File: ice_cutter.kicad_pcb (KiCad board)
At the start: 4 copper layers, 90 x 100 mm, 184 parts, among them J1 Conn_01x01_Male, J2 Barrel_Jack, J3 pot, J4 Conn_01x01_Male, J5 program, J6 program2, J7 hands, J8 UART, J9 xt60, M1 Motor_Servo, M2 Motor_Servo, Q1 Q_PMOS_GSD, Q10 S8050_SMD, Q11 Q_NMOS_GSD, Q12 Q_NMOS_GSD, Q13 Q_NMOS_GSD, Q14 Q_NMOS_GSD, Q15 S8550, Q16 S8050_SMD, Q17 S8050_SMD, Q18 S8050_SMD, Q2 Q_PMOS_GSD, Q3 Q_PMOS_GSD, Q4 S8550, Q5 Q_NMOS_GSD, Q6 S8550, Q7 Q_NMOS_GSD, Q8 S8050_SMD, Q9 S8050_SMD, SW1 SW_Push, SW2 SW_Push, SW3 SW_Push, U1 LM317_TO-252, U10 TMP117, U11 TM1620, U12 INA219AxD, U2 LM317_TO-252, U3 INA219AxD, U4 LM317_TO-252, U5 INA219AxD, U6 FJ4301AH, U7 FJ4301AH, U8 STM32G030XX, U9 SHT30-DIS

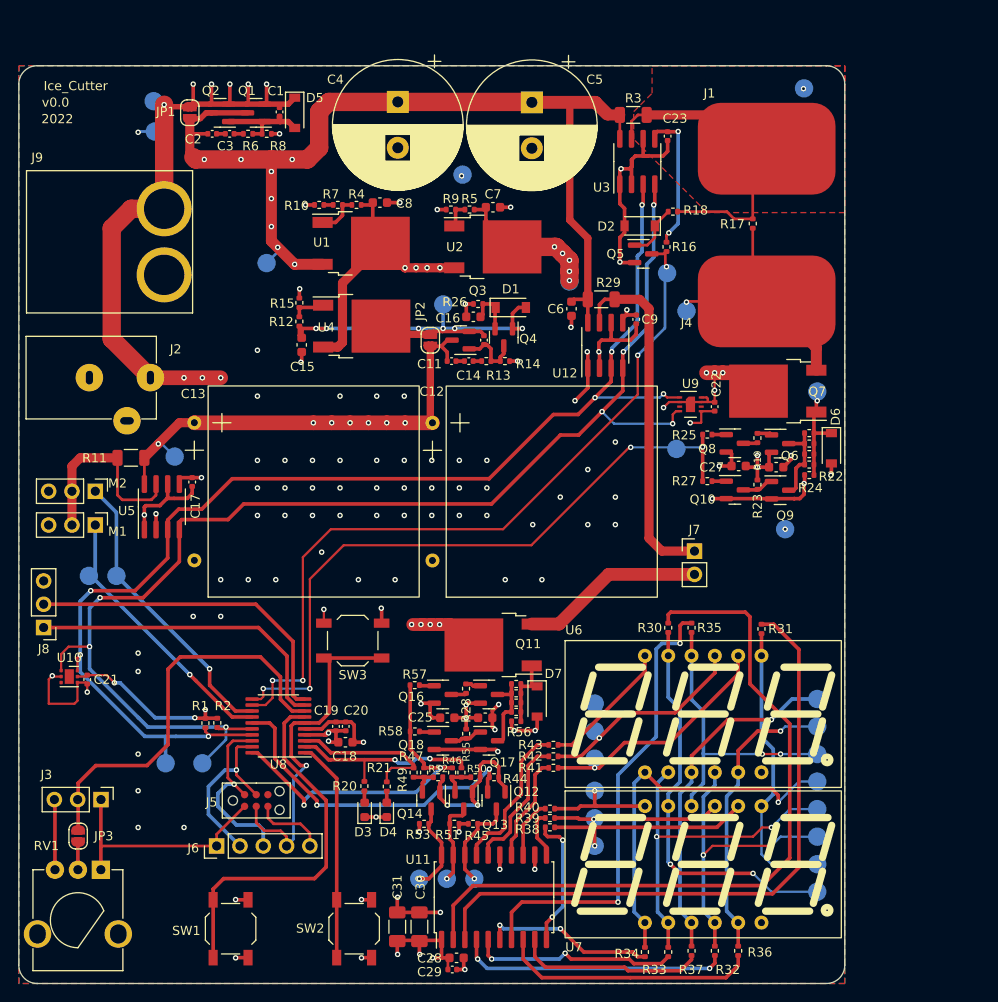
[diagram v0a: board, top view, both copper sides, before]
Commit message: improved schematic and changed the shunt resistors
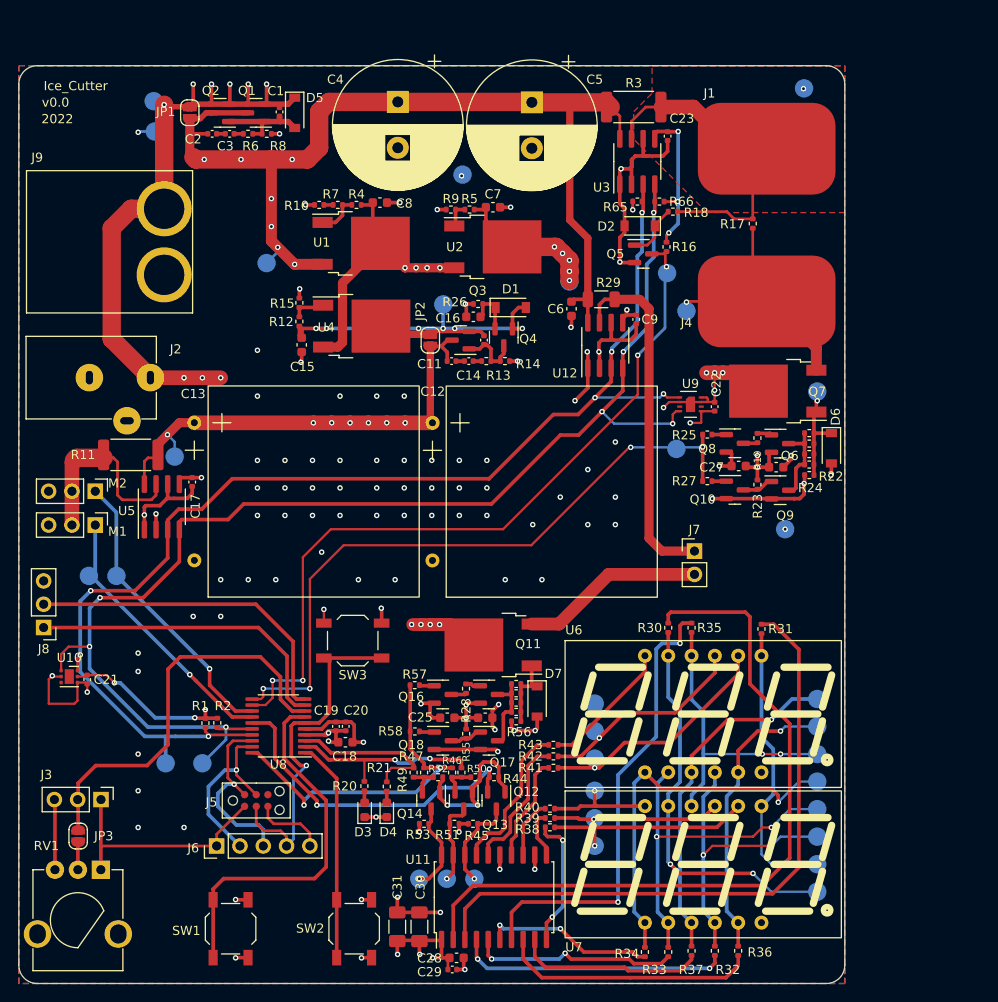
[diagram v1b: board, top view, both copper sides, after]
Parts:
- added R65: 4k7, Resistor_SMD:R_0402_1005Metric, F.Cu at (135.8, 44.2)
- added R66: 4k7, Resistor_SMD:R_0402_1005Metric, F.Cu at (138.2, 44.2)
- C4, C5: value 1m -> 4.7m
- R11, R3: value 0R1 -> 15mR; footprint Resistor_SMD:R_1206_3216Metric -> Resistor_SMD:R_2512_6332Metric
- R18: value 100R -> 330R
- moved R3 0.86 mm to (135.4, 33.9)
- moved R11 0.32 mm to (80.6, 71.8)
- turned R18 to 180 degrees
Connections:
- R18 pad 1: Net-(D2-Pad1) -> /Wire_H
- R18 pad 2: /Wire_H -> Net-(D2-Pad1)
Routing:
- net +3V3: track 155.8 -> 158.4 mm, vias 20 -> 22
- net /5V_SS: track 67.0 -> 68.0 mm
- net /Wire_H: track 35.3 -> 36.0 mm
- net /V_SS: track 111.8 -> 111.9 mm, vias 8 -> 7

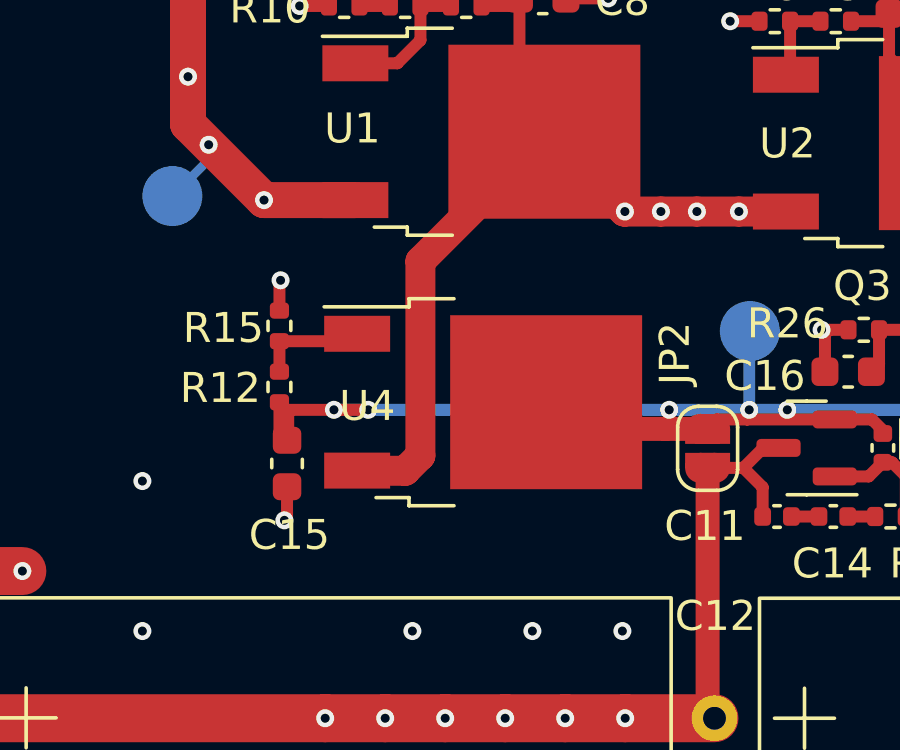
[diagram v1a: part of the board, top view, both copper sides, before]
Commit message: modified the system to operate on 5V - bypassed all regs and changed the BIG FET to a lower threshold V
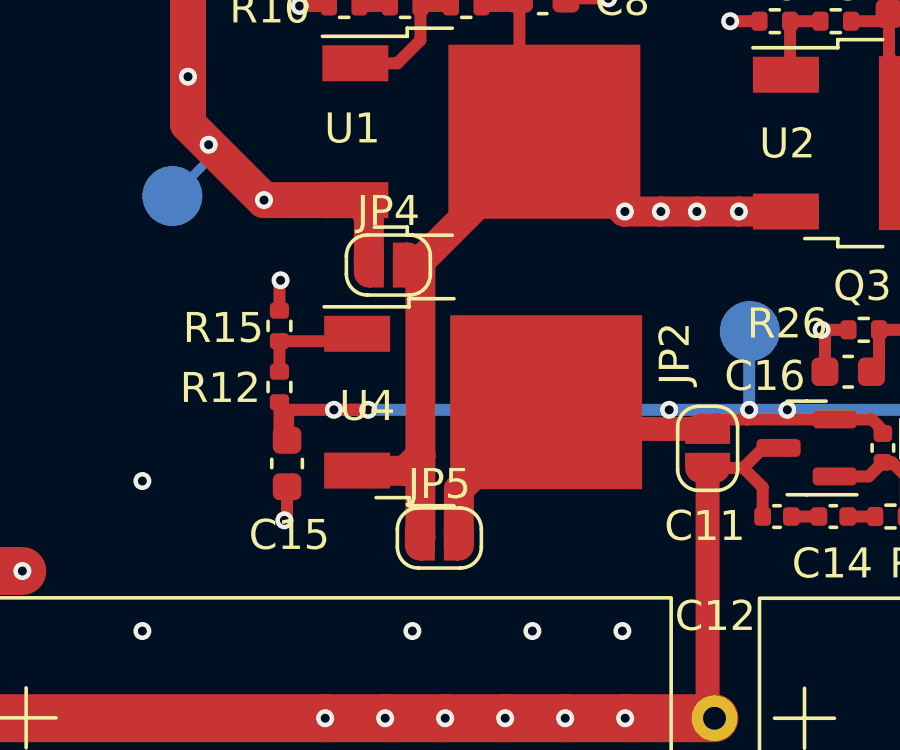
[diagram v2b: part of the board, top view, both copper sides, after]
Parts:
- added JP4: Jumper_2_Open, Jumper:SolderJumper-2_P1.3mm_Open_RoundedPad1.0x1.5mm, F.Cu at (102.6, 53.2)
- added JP5: Jumper_2_Open, Jumper:SolderJumper-2_P1.3mm_Open_RoundedPad1.0x1.5mm, F.Cu at (104.3, 62.3)
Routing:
- net +5V: track 47.7 -> 53.4 mm
- net +12V: track 149.2 -> 151.9 mm
- net /V_SS: track 111.9 -> 114.2 mm
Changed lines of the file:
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@@
     )
   )
+  (footprint "Jumper:SolderJumper-2_P1.3mm_Open_RoundedPad1.0x1.5mm" (layer "F.Cu")
+    (at 102.564 53.213)
+    (descr "SMD Solder Jumper, 1x1.5mm, rounded Pads, 0.3mm gap, open")
+    (tags "solder jumper open")
+    (property "Extended" "0")
+    (property "Populate" "No")
+    (property "Sheetfile" "ice_cutter.kicad_sch")
+    (property "Sheetname" "")
+    (attr exclude_from_pos_files)
+    (fp_text reference "JP4" (at 0 -1.8) (layer "F.SilkS")
+      (effects (font (size 1 1) (thickness 0.15)))
+    )
+    (fp_text value "Jumper_2_Open" (at 0 1.9) (layer "F.Fab")
+      (effects (font (size 1 1) (thickness 0.15)))
+    )
+    (fp_line (start -1.4 0.3) (end -1.4 -0.3) (layer "F.SilkS") (width 0.12))
+    (fp_line (start 1.4 -0.3) (end 1.4 0.3) (layer "F.SilkS") (width 0.12))
+    (fp_line (start -0.7 -1) (end 0.7 -1) (layer "F.SilkS") (width 0.12))
+    (fp_line (start 0.7 1) (end -0.7 1) (layer "F.SilkS") (width 0.12))
+    (fp_arc (start -1.4 -0.3) (mid -1.194975 -0.794975) (end -0.7 -1) (layer "F.SilkS") (width 0.12))
+    (fp_arc (start -0.7 1) (mid -1.194975 0.794975) (end -1.4 0.3) (layer "F.SilkS") (width 0.12))
+    (fp_arc (start 1.4 0.3) (mid 1.194975 0.794975) (end 0.7 1) (layer "F.SilkS") (width 0.12))
+    (fp_arc (start 0.7 -1) (mid 1.194975 -0.794975) (end 1.4 -0.3) (layer "F.SilkS") (width 0.12))
+    (fp_line (start -1.65 -1.25) (end 1.65 -1.25) (layer "F.CrtYd") (width 0.05))
+    (fp_line (start 1.65 1.25) (end -1.65 1.25) (layer "F.CrtYd") (width 0.05))
+    (fp_line (start -1.65 -1.25) (end -1.65 1.25) (layer "F.CrtYd") (width 0.05))
+    (fp_line (start 1.65 1.25) (end 1.65 -1.25) (layer "F.CrtYd") (width 0.05))
+    (pad "1" smd custom locked (at -0.65 0) (size 1 0.5) (layers "F.Cu" "F.Mask")
+      (net 3 "/V_SS") (pinfunction "A") (pintype "passive") (zone_connect 2)
+      (options (clearance outline) (anchor rect))
+      (primitives
+        (gr_circle (center 0 0.25) (end 0.5 0.25) (width 0) (fill yes))
+        (gr_circle (center 0 -0.25) (end 0.5 -0.25) (width 0) (fill yes))
+        (gr_poly (pts
+            (xy 0.5 0.75)
+            (xy 0 0.75)
+            (xy 0 -0.75)
+            (xy 0.5 -0.75)
+          ) (width 0) (fill yes))
+      ))
+    (pad "2" smd custom locked (at 0.65 0) (size 1 0.5) (layers "F.Cu" "F.Mask")
+      (net 8 "+12V") (pinfunction "B") (pintype "passive") (zone_connect 2)
+      (options (clearance outline) (anchor rect))
+      (primitives
+        (gr_circle (center 0 0.25) (end 0.5 0.25) (width 0) (fill yes))
+        (gr_circle (center 0 -0.25) (end 0.5 -0.25) (width 0) (fill yes))
+        (gr_poly (pts
+            (xy 0 0.75)
+            (xy -0.5 0.75)
+            (xy -0.5 -0.75)
+            (xy 0 -0.75)
+          ) (width 0) (fill yes))
+      ))
+  )
   (footprint "Capacitor_THT:CP_Radial_D14.0mm_P5.00mm" (layer "F.Cu")
     (at 124.265 33.401 -90)
@@
     )
   )
+  (footprint "Jumper:SolderJumper-2_P1.3mm_Open_RoundedPad1.0x1.5mm" (layer "F.Cu")
+    (at 104.264 62.313)
+    (descr "SMD Solder Jumper, 1x1.5mm, rounded Pads, 0.3mm gap, open")
+    (tags "solder jumper open")
+    (property "Extended" "0")
+    (property "Populate" "No")
+    (property "Sheetfile" "ice_cutter.kicad_sch")
+    (property "Sheetname" "")
+    (attr exclude_from_pos_files)
+    (fp_text reference "JP5" (at 0 -1.8) (layer "F.SilkS")
+      (effects (font (size 1 1) (thickness 0.15)))
+    )
+    (fp_text value "Jumper_2_Open" (at 0 1.9) (layer "F.Fab")
+      (effects (font (size 1 1) (thickness 0.15)))
+    )
+    (fp_line (start -1.4 0.3) (end -1.4 -0.3) (layer "F.SilkS") (width 0.12))
+    (fp_line (start 0.7 1) (end -0.7 1) (layer "F.SilkS") (width 0.12))
+    (fp_line (start 1.4 -0.3) (end 1.4 0.3) (layer "F.SilkS") (width 0.12))
+    (fp_line (start -0.7 -1) (end 0.7 -1) (layer "F.SilkS") (width 0.12))
+    (fp_arc (start -0.7 1) (mid -1.194975 0.794975) (end -1.4 0.3) (layer "F.SilkS") (width 0.12))
+    (fp_arc (start -1.4 -0.3) (mid -1.194975 -0.794975) (end -0.7 -1) (layer "F.SilkS") (width 0.12))
+    (fp_arc (start 0.7 -1) (mid 1.194975 -0.794975) (end 1.4 -0.3) (layer "F.SilkS") (width 0.12))
+    (fp_arc (start 1.4 0.3) (mid 1.194975 0.794975) (end 0.7 1) (layer "F.SilkS") (width 0.12))
+    (fp_line (start 1.65 1.25) (end -1.65 1.25) (layer "F.CrtYd") (width 0.05))
+    (fp_line (start 1.65 1.25) (end 1.65 -1.25) (layer "F.CrtYd") (width 0.05))
+    (fp_line (start -1.65 -1.25) (end -1.65 1.25) (layer "F.CrtYd") (width 0.05))
+    (fp_line (start -1.65 -1.25) (end 1.65 -1.25) (layer "F.CrtYd") (width 0.05))
+    (pad "1" smd custom locked (at -0.65 0) (size 1 0.5) (layers "F.Cu" "F.Mask")
+      (net 8 "+12V") (pinfunction "A") (pintype "passive") (zone_connect 2)
+      (options (clearance outline) (anchor rect))
+      (primitives
+        (gr_circle (center 0 0.25) (end 0.5 0.25) (width 0) (fill yes))
+        (gr_circle (center 0 -0.25) (end 0.5 -0.25) (width 0) (fill yes))
+        (gr_poly (pts
+            (xy 0.5 0.75)
+            (xy 0 0.75)
+            (xy 0 -0.75)
+            (xy 0.5 -0.75)
+          ) (width 0) (fill yes))
+      ))
+    (pad "2" smd custom locked (at 0.65 0) (size 1 0.5) (layers "F.Cu" "F.Mask")
+      (net 9 "+5V") (pinfunction "B") (pintype "passive") (zone_connect 2)
+      (options (clearance outline) (anchor rect))
+      (primitives
+        (gr_circle (center 0 0.25) (end 0.5 0.25) (width 0) (fill yes))
+        (gr_circle (center 0 -0.25) (end 0.5 -0.25) (width 0) (fill yes))
+        (gr_poly (pts
+            (xy 0 0.75)
+            (xy -0.5 0.75)
+            (xy -0.5 -0.75)
+            (xy 0 -0.75)
+          ) (width 0) (fill yes))
+      ))
+  )
   (footprint "Diode_SMD:D_0603_1608Metric" (layer "F.Cu")
     (at 106.045 110.49 90)
@@
     (tags "DPAK TO-252 DPAK-3 TO-252-3 SOT-428")
     (property "Extended" "1")
-    (property "LCSC" "C130980")
+    (property "LCSC" "C709962")
     (property "Populate" "Yes")
     (property "Price" "0.2")
@@
     (tags "DPAK TO-252 DPAK-3 TO-252-3 SOT-428")
     (property "Extended" "1")
-    (property "LCSC" "C130980")
+    (property "LCSC" "C709962")
     (property "Populate" "Yes")
     (property "Price" "0.2")
@@
   (segment (start 132.352 33.401) (end 132.864 33.913) (width 2) (layer "F.Cu") (net 3))
   (segment (start 86.995 35.179) (end 88.138 35.179) (width 0.6) (layer "F.Cu") (net 3))
+  (segment (start 101.914 51.498) (end 101.464 51.048) (width 1) (layer "F.Cu") (net 3))
   (segment (start 93.285 34.544) (end 89.3595 34.544) (width 0.6) (layer "F.Cu") (net 3))
   (segment (start 101.092 38.354) (end 101.092 34.417) (width 2) (layer "F.Cu") (net 3))
@@
   (segment (start 130.3635 48.1945) (end 128.397 46.228) (width 0.8) (layer "F.Cu") (net 3))
   (segment (start 88.956 36.83) (end 87.122 36.83) (width 0.4) (layer "F.Cu") (net 3))
+  (segment (start 101.914 53.213) (end 101.914 51.498) (width 1) (layer "F.Cu") (net 3))
   (segment (start 86.995 38.989) (end 86.995 35.179) (width 1) (layer "F.Cu") (net 3))
   (via (at 95.885 43.892) (size 0.6) (drill 0.3) (layers "F.Cu" "B.Cu") (net 3))
@@
   (segment (start 150.114 71.803) (end 150.114 73.152) (width 0.4) (layer "F.Cu") (net 8))
   (segment (start 150.114 73.152) (end 148.717 73.152) (width 0.4) (layer "F.Cu") (net 8))
+  (segment (start 103.614 62.313) (end 103.632 62.295) (width 1) (layer "F.Cu") (net 8))
   (segment (start 150.383 71.534) (end 150.114 71.803) (width 0.4) (layer "F.Cu") (net 8))
   (segment (start 147.701 73.152) (end 147.574 73.025) (width 0.4) (layer "F.Cu") (net 8))
@@
   (segment (start 101.529 60.071) (end 101.523 60.065) (width 1) (layer "F.Cu") (net 8))
   (segment (start 106.934 44.323) (end 106.934 47.938) (width 0.4) (layer "F.Cu") (net 8))
+  (segment (start 103.632 62.295) (end 103.632 59.563) (width 1) (layer "F.Cu") (net 8))
   (segment (start 103.124 60.071) (end 101.529 60.071) (width 1) (layer "F.Cu") (net 8))
   (segment (start 148.717 73.152) (end 147.701 73.152) (width 0.4) (layer "F.Cu") (net 8))
@@
   (segment (start 123.6175 55.753) (end 122.809 55.753) (width 0.4) (layer "F.Cu") (net 9))
   (segment (start 114.592 58.039) (end 114.592 58.293) (width 0.4) (layer "F.Cu") (net 9))
+  (segment (start 104.914 62.313) (end 104.914 60.694) (width 1) (layer "F.Cu") (net 9))
   (segment (start 99.225 58.039) (end 101.892 58.039) (width 0.4) (layer "F.Cu") (net 9))
   (segment (start 108.712 58.674) (end 111.798 58.674) (width 0.8) (layer "F.Cu") (net 9))
   (segment (start 114.592 58.293) (end 114.526 58.359) (width 0.4) (layer "F.Cu") (net 9))
   (segment (start 119.0475 58.7225) (end 118.684 58.359) (width 0.4) (layer "F.Cu") (net 9))
+  (segment (start 104.914 60.694) (end 107.823 57.785) (width 1) (layer "F.Cu") (net 9))
   (segment (start 123.198 58.069) (end 123.228 58.039) (width 0.4) (layer "F.Cu") (net 9))
   (segment (start 119.0475 58.829) (end 119.0475 58.7225) (width 0.4) (layer "F.Cu") (net 9))
